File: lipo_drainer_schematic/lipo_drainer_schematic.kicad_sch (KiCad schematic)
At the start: 57 parts, among them J1 BATT, J2 Vcal, J3 128x64_OLED, J4 Gcal, J5 Ical, Q1 MMBT3904, Q2 IRLML5103TRPBF, Q3 MMBT3904, Q4 FQP27P06, Q5 FQP27P06, Q6 MMBT3904, Q7 FQP27P06, Q8 FQP27P06, SW1 BT1, SW2 BT2, SW3 BT3, SW4 BT4, SW5 ON, SW6 RUN, U1 LM2936-3.3_TO92, U2 Pico, U3 LM4040DBZ-3, U4 LM4040DBZ-3

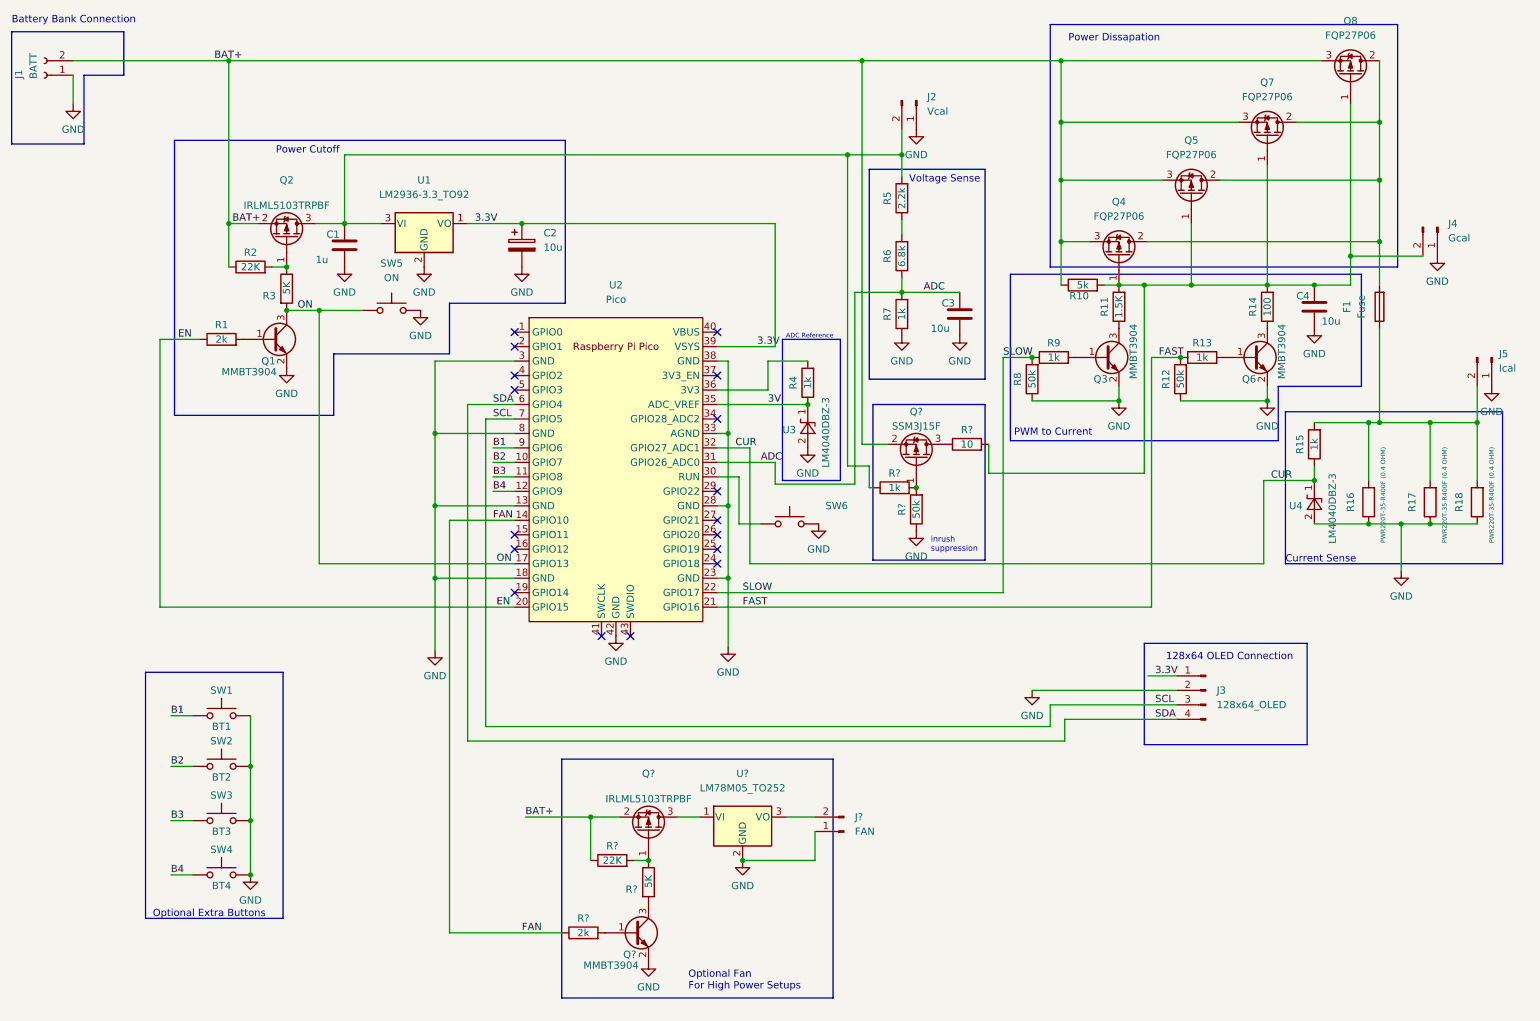
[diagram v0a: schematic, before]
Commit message: Added flyback diode to fan control
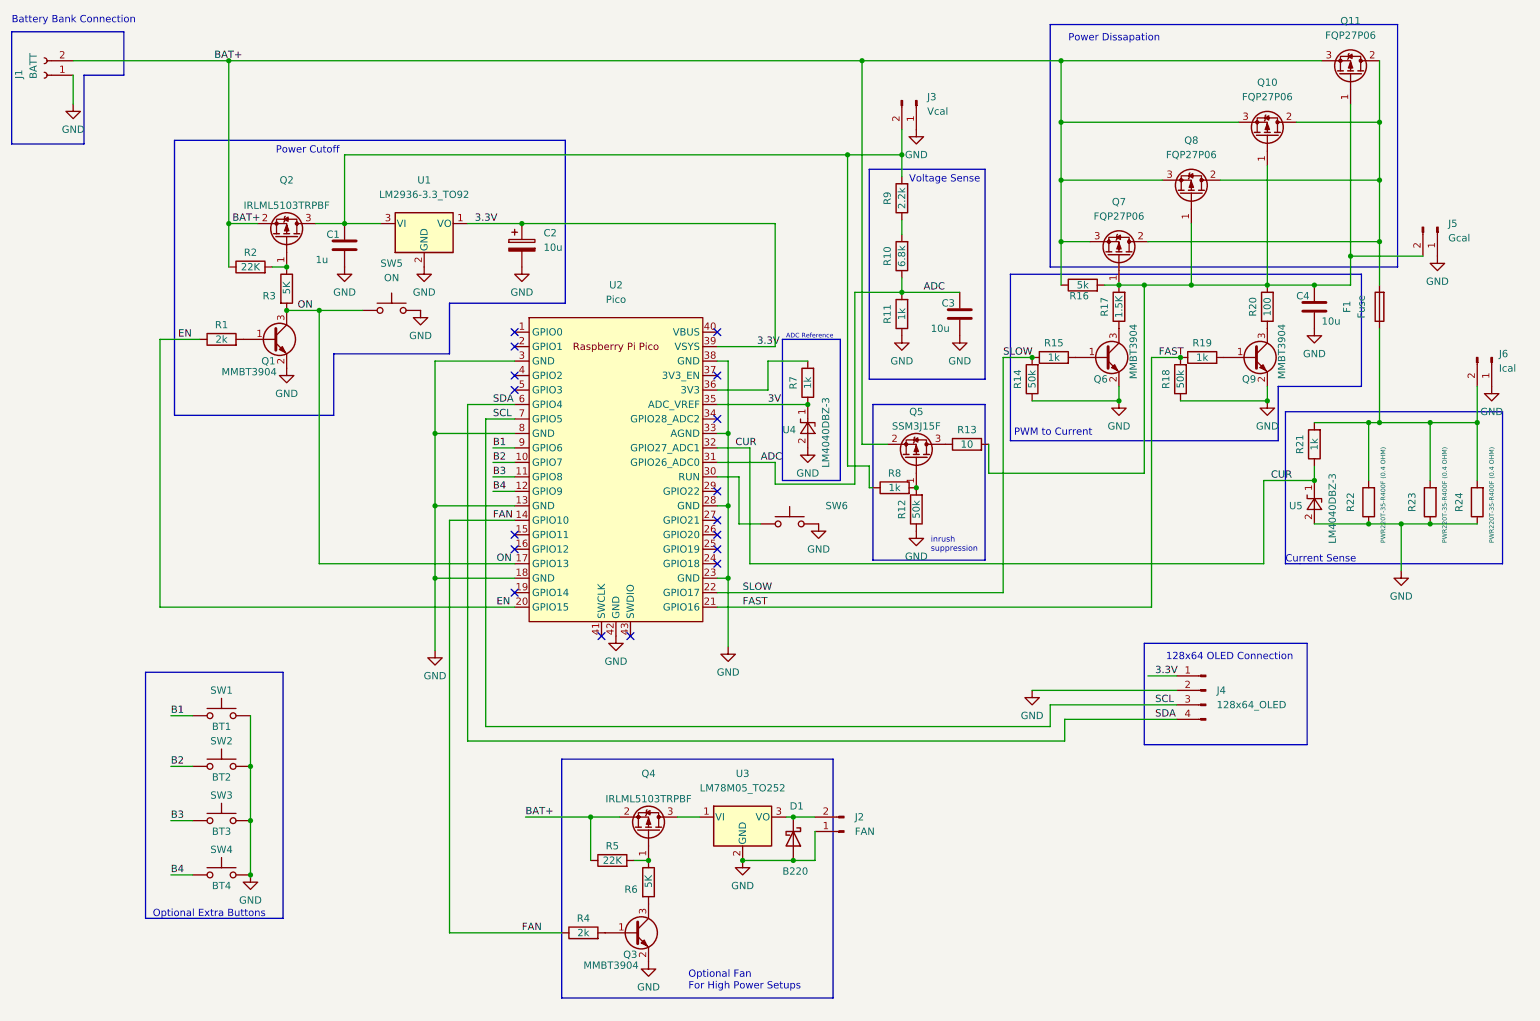
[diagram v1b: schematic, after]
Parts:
- added D1: B220, Diode_SMD:D_SMB, symbol Diode:B220
- gave numbers to parts that had none: 11
- renumbered J2 to J3, J3 to J4, J4 to J5, J5 to J6, Q7 to Q10, Q8 to Q11, Q3 to Q6, Q4 to Q7, Q5 to Q8, Q6 to Q9, R6 to R10, R7 to R11, R8 to R14, R9 to R15, R10 to R16, R11 to R17, R12 to R18, R13 to R19, R14 to R20, R15 to R21, R16 to R22, R17 to R23, R18 to R24, R4 to R7, R5 to R9, U3 to U4, U4 to U5
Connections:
- net GND: now also D1.2 (A)
- net at J2.2 (Pin_2), U3.3 (VO): now also D1.1 (K)

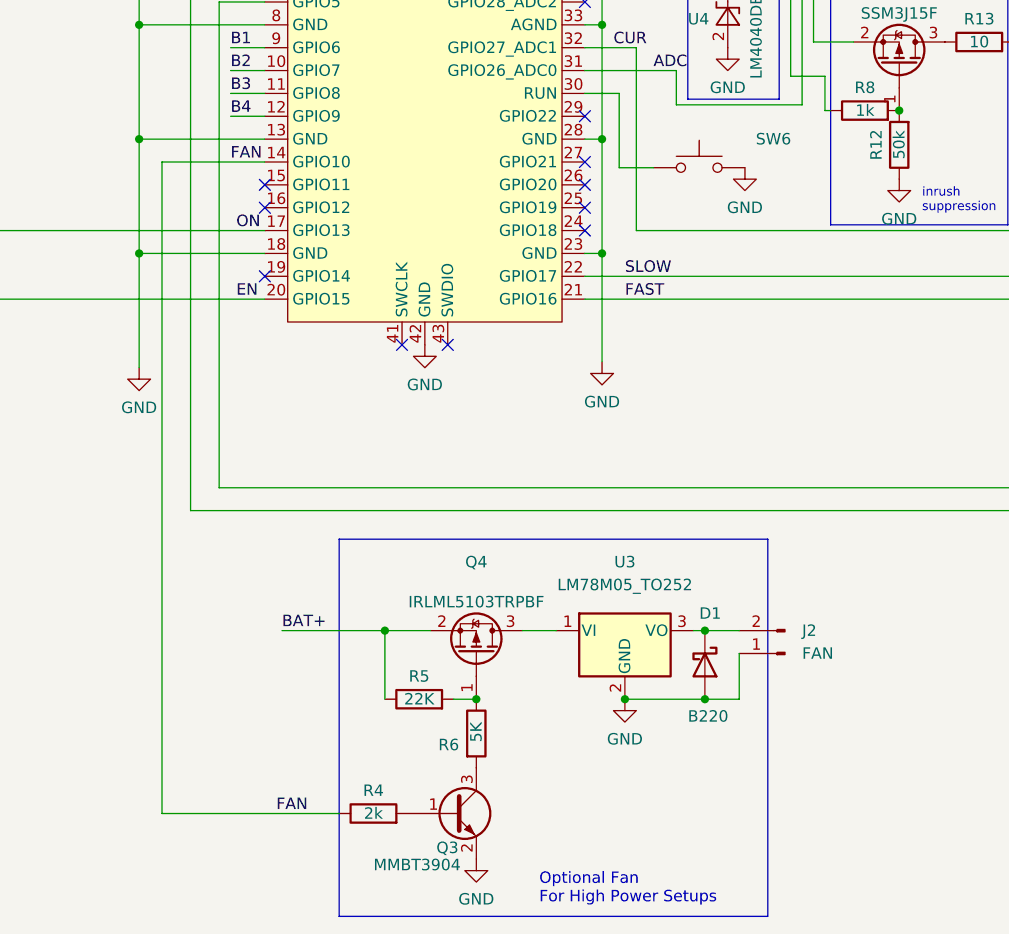
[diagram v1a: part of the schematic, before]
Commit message: Switched fan control regulator to one with an enable pin.
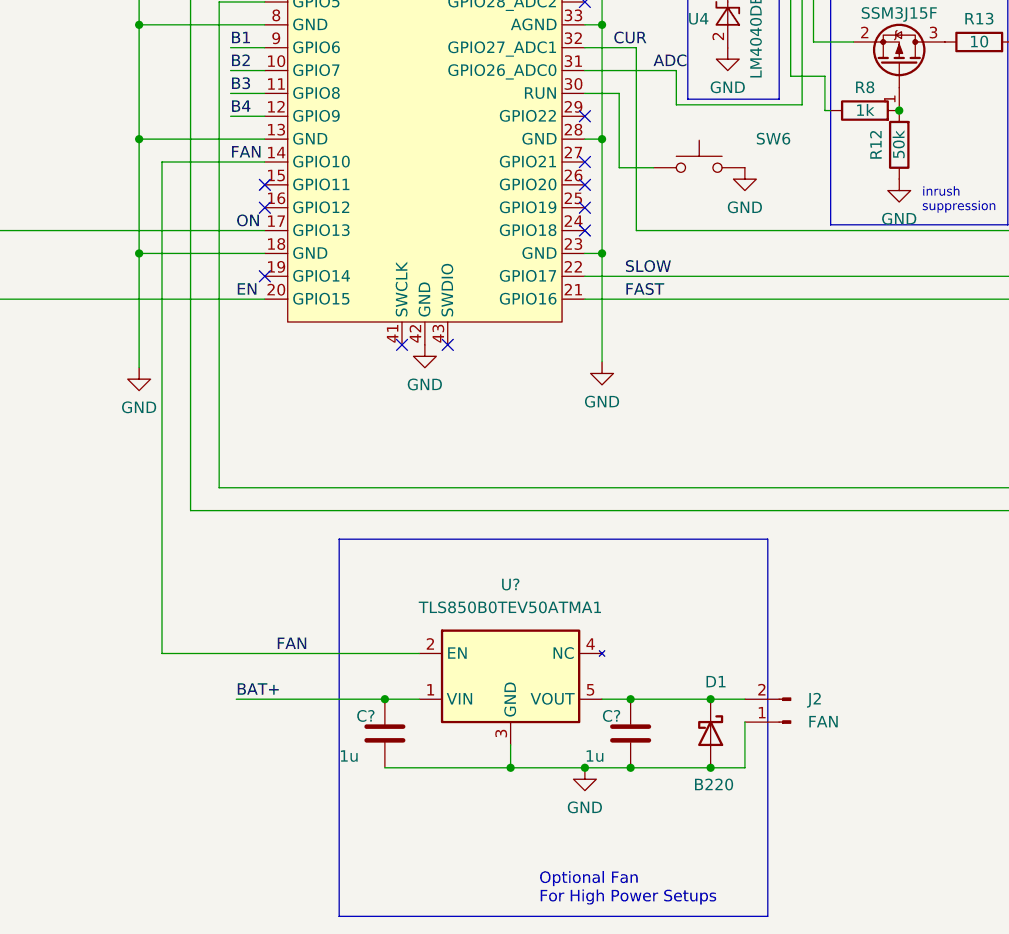
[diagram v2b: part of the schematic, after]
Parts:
- removed Q3: MMBT3904, Package_TO_SOT_SMD:SOT-23, symbol Transistor_BJT:MMBT3904
- removed Q4: IRLML5103TRPBF, Package_TO_SOT_SMD:SOT-23, symbol Transistor_FET:BSS84
- removed R4: 2k, Resistor_SMD:R_0805_2012Metric_Pad1.20x1.40mm_HandSolder, symbol Device:R
- removed R5: 22K, Resistor_SMD:R_0805_2012Metric_Pad1.20x1.40mm_HandSolder, symbol Device:R
- removed R6: 5K, Resistor_SMD:R_0805_2012Metric_Pad1.20x1.40mm_HandSolder, symbol Device:R
- removed U3: LM78M05_TO252, Package_TO_SOT_SMD:TO-252-2, symbol Regulator_Linear:LM78M05_TO252
- added C? (x2): 1u, symbol Device:C
- added U?: TLS850B0TEV50ATMA1, Package_TO_SOT_SMD:TO-252-5_TabPin3, symbol Regulator_Linear:MIC29152WU
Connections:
- net BAT+: now also C?.1, U?.1 (VIN)
- net FAN: now also U?.2 (EN)
- net GND: now also C?.2, C?.2, U?.3 (GND)
- net at D1.1 (K), J2.2 (Pin_2): now also C?.1, U?.5 (VOUT)
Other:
- moved on the sheet: D1, J2

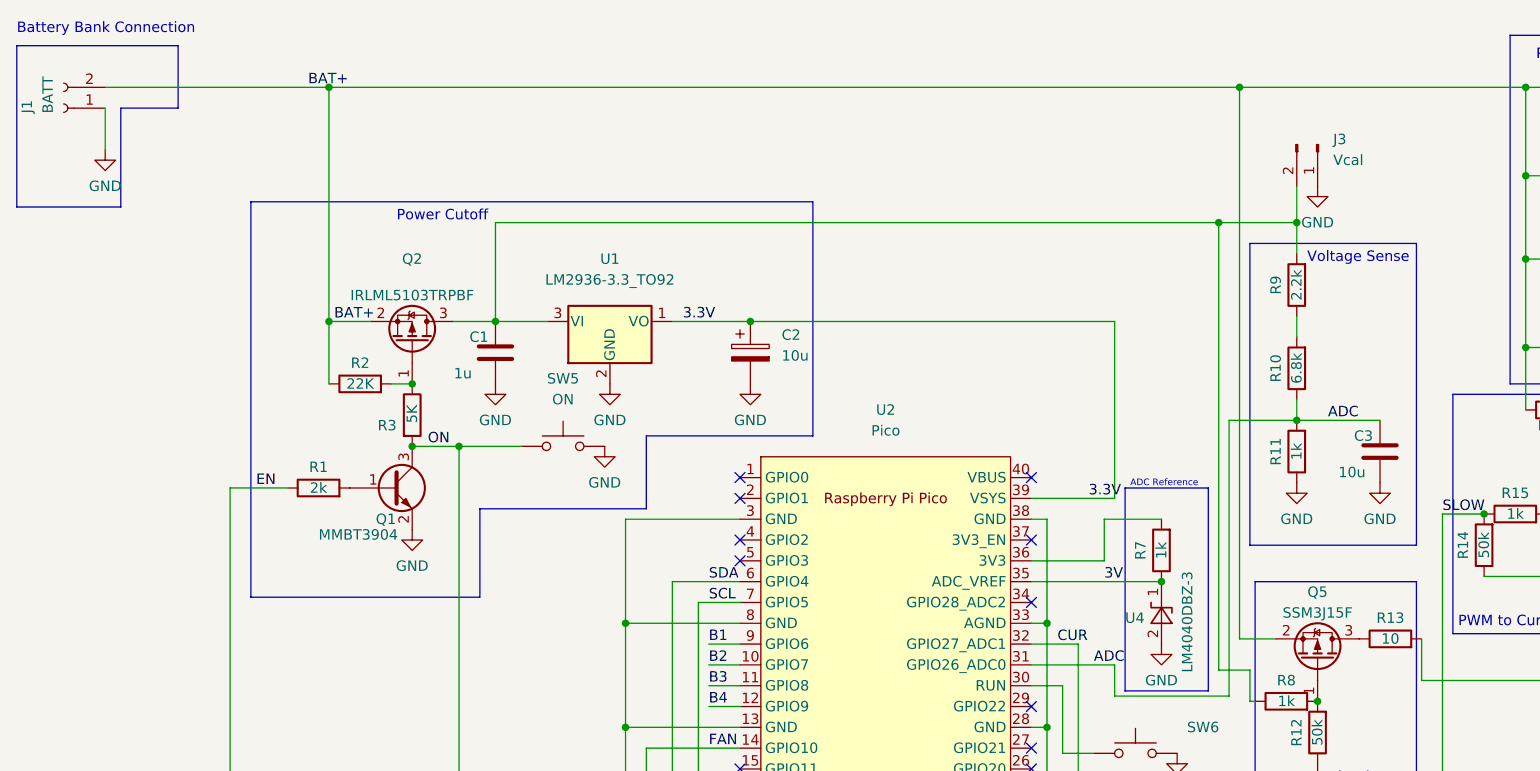
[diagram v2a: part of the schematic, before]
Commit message: Changed transistor for less individual parts
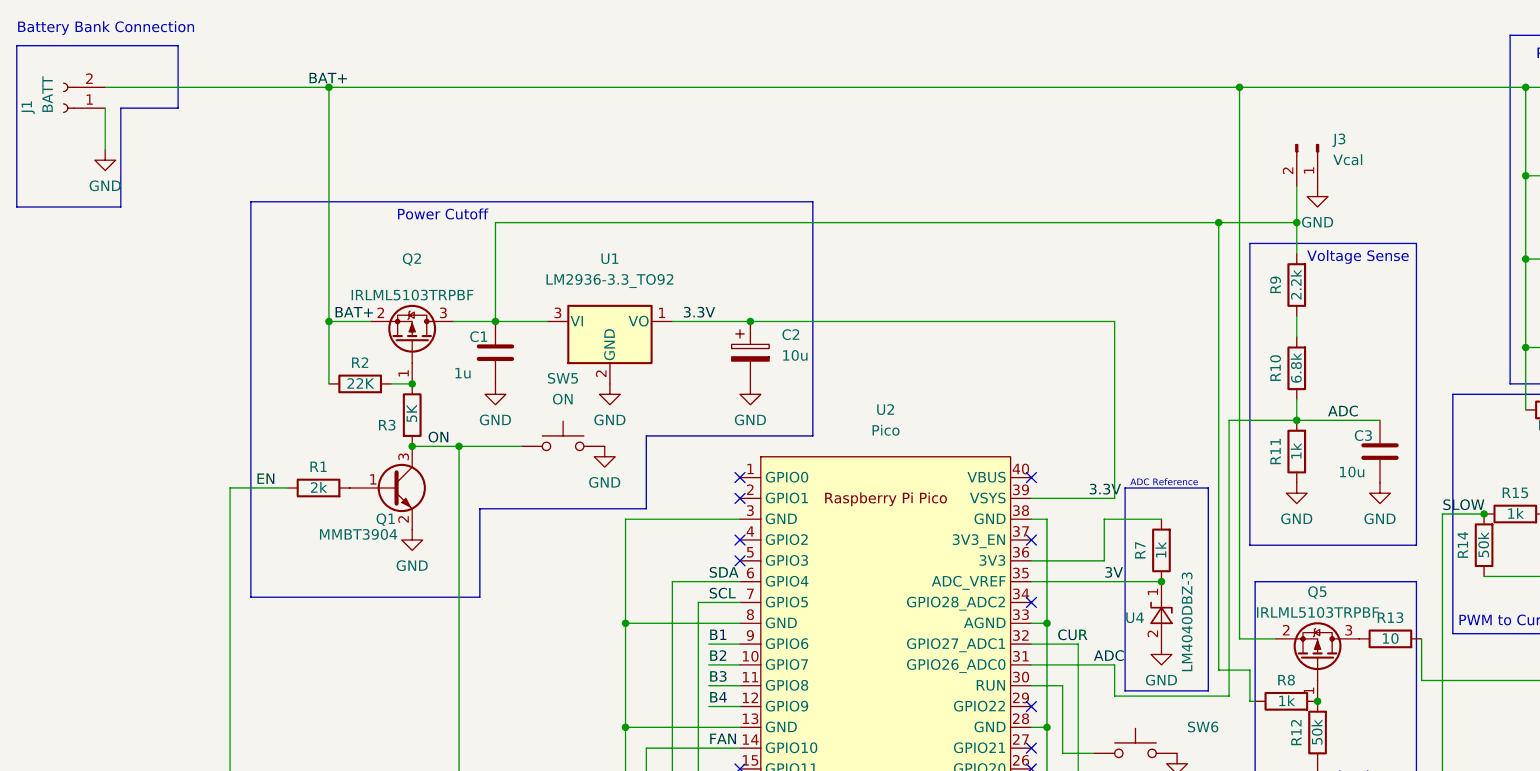
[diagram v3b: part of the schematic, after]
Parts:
- Q5: value SSM3J15F -> IRLML5103TRPBF

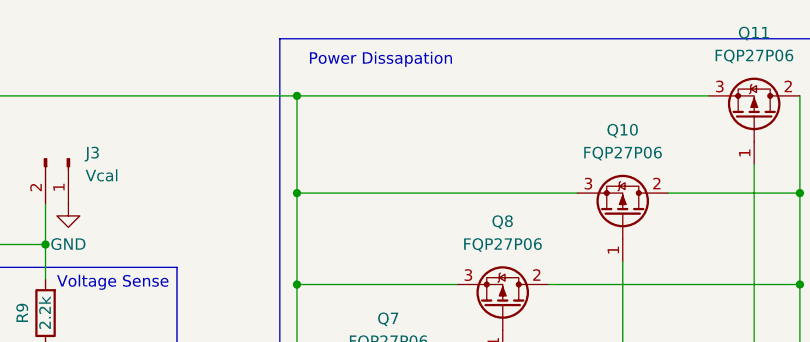
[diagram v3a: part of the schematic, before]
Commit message: Added documenation for schematic.
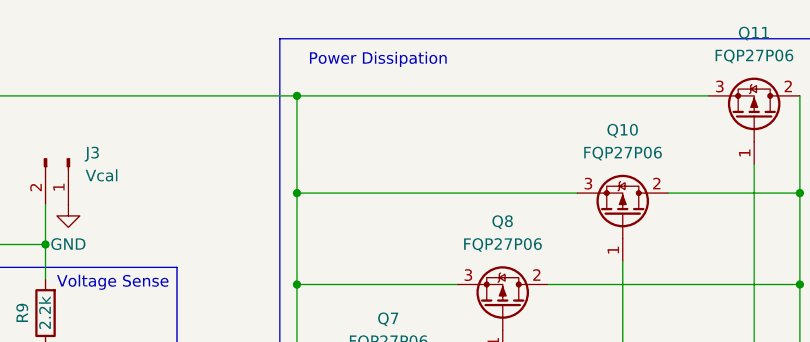
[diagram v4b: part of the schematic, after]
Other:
- note added: "Power Dissipation"
- note removed: "Power Dissapation"
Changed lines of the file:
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@@
     (effects (font (size 1.27 1.27)) (justify left bottom))
   )
-  (text "Power Dissapation" (at 203.835 24.13 0)
+  (text "Power Dissipation" (at 203.835 24.13 0)
     (effects (font (size 1.27 1.27)) (justify left bottom))
   )
